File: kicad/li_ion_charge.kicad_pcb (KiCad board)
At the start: 2 copper layers, 31.9 x 25.9 mm, 18 parts, among them P101 USB_B, P102 CONN_01X02, P103 CONN_01X02, U101 MCP73834-FCI/UN

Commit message: add a couple vias
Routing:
- net (no net): track 0.97 -> 5.54 mm, vias 0 -> 3
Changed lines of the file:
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@@
     (links 38)
     (no_connects 0)
-    (area 86.062199 43.772899 177.985734 113.985733)
+    (area 86.062199 43.772899 177.310734 113.985733)
     (thickness 1.6)
     (drawings 6)
-    (tracks 54)
+    (tracks 59)
     (zones 0)
     (modules 18)
@@
   )
   (setup
-    (last_trace_width 0.3048)
+    (last_trace_width 0.6096)
     (user_trace_width 0.3048)
     (user_trace_width 0.6096)
@@
   (segment (start 86.3396 44.0503) (end 86.3396 44.7396) (width 0.25) (layer F.Cu) (net 0))
   (segment (start 96.6 58.05) (end 96.4 58.25) (width 0.25) (layer F.Cu) (net 0))
+  (via (at 144.018 87.63) (size 0.6858) (drill 0.3302) (layers F.Cu B.Cu) (net 0))
+  (via (at 144.018 92.202) (size 0.6858) (drill 0.3302) (layers F.Cu B.Cu) (net 0))
+  (segment (start 144.018 92.202) (end 144.018 90.17) (width 0.6096) (layer F.Cu) (net 0))
+  (via (at 144.018 90.17) (size 0.6858) (drill 0.3302) (layers F.Cu B.Cu) (net 0))
+  (segment (start 144.018 90.17) (end 144.018 87.63) (width 0.6096) (layer B.Cu) (net 0))
   (segment (start 167.125 102.875) (end 169.05 102.875) (width 0.3048) (layer F.Cu) (net 1))
   (segment (start 168.325 103.75) (end 157.825 103.75) (width 0.3048) (layer B.Cu) (net 1))
@@
   (segment (start 159.7 94.65) (end 161 94.65) (width 0.25) (layer F.Cu) (net 6))
   (segment (start 158.875 93.825) (end 159.7 94.65) (width 0.25) (layer F.Cu) (net 6))
-  (segment (start 144 93.975) (end 144 96) (width 0.3048) (layer F.Cu) (net 8))
-  (segment (start 143.875 93.85) (end 144 93.975) (width 0.3048) (layer F.Cu) (net 8))
-  (via (at 143.875 93.85) (size 0.6858) (drill 0.3302) (layers F.Cu B.Cu) (net 8))
-  (segment (start 143.875 93.8) (end 143.875 93.85) (width 0.3048) (layer B.Cu) (net 8))
-  (segment (start 144.6 93.075) (end 143.875 93.8) (width 0.6096) (layer B.Cu) (net 8))
+  (segment (start 144.143 94.105) (end 144 96) (width 0.3048) (layer F.Cu) (net 8))
+  (via (at 160.075 93.1) (size 0.6858) (drill 0.3302) (layers F.Cu B.Cu) (net 8))
+  (segment (start 160.075 93.1) (end 160.05 93.075) (width 0.3048) (layer B.Cu) (net 8))
   (segment (start 160.05 93.075) (end 144.6 93.075) (width 0.6096) (layer B.Cu) (net 8))
-  (segment (start 160.075 93.1) (end 160.05 93.075) (width 0.3048) (layer B.Cu) (net 8))
-  (via (at 160.075 93.1) (size 0.6858) (drill 0.3302) (layers F.Cu B.Cu) (net 8))
+  (segment (start 144.6 93.075) (end 144.018 93.93) (width 0.6096) (layer B.Cu) (net 8))
+  (segment (start 144.018 93.93) (end 144.018 93.98) (width 0.3048) (layer B.Cu) (net 8))
+  (via (at 144.018 93.98) (size 0.6858) (drill 0.3302) (layers F.Cu B.Cu) (net 8))
+  (segment (start 144.018 93.98) (end 144.143 94.105) (width 0.3048) (layer F.Cu) (net 8))
   (segment (start 143.9 107) (end 143.9 108.9) (width 0.3048) (layer F.Cu) (net 8))
   (segment (start 143.9 108.9) (end 146.175 111.175) (width 0.3048) (layer F.Cu) (net 8))

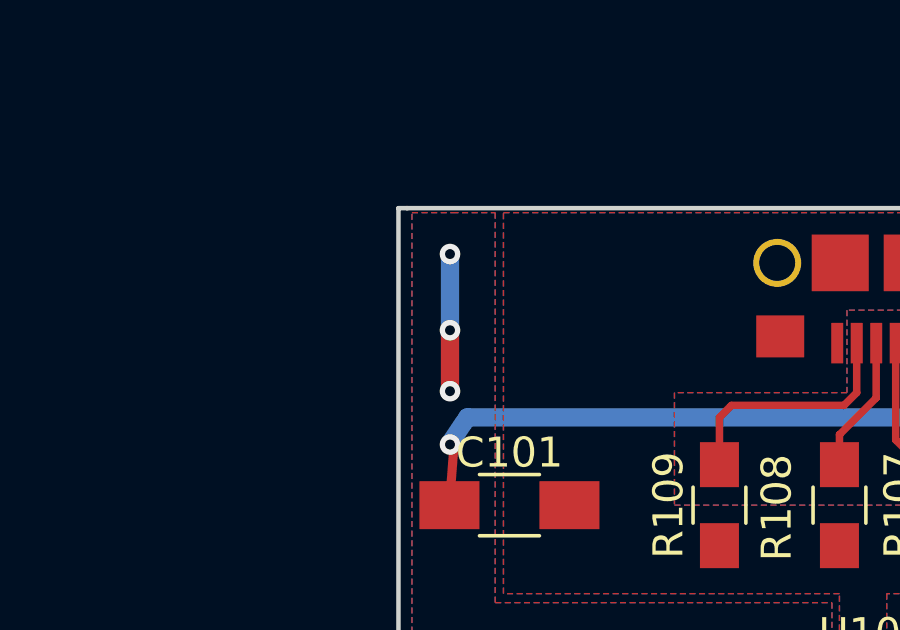
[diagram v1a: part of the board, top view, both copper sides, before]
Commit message: add stitching via footprint
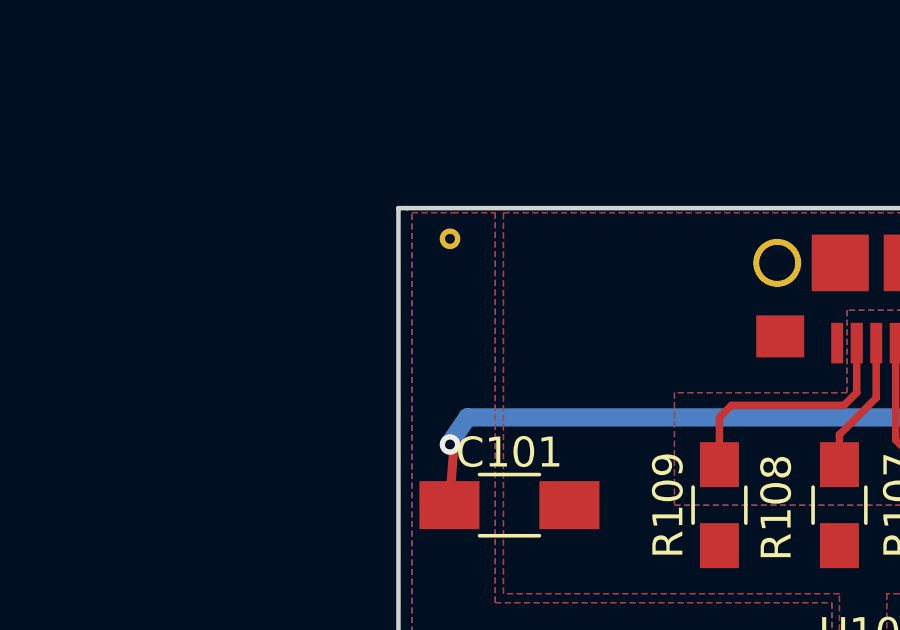
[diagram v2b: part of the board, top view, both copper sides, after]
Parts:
- added REF**: stitching_via, li_ion_charge_library:stitching_via, F.Cu at (144.0, 87.1)
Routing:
- net (no net): track 5.54 -> 0.97 mm, vias 3 -> 0
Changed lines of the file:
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@@
 (kicad_pcb (version 4) (host pcbnew 4.0.6-e0-6349~53~ubuntu14.04.1)
   (general
-    (links 38)
+    (links 39)
     (no_connects 0)
     (area 86.062199 43.772899 177.310734 113.985733)
     (thickness 1.6)
     (drawings 6)
-    (tracks 59)
+    (tracks 54)
     (zones 0)
-    (modules 18)
+    (modules 19)
     (nets 16)
   )
@@
     (mod_text_size 1 1)
     (mod_text_width 0.15)
-    (pad_size 1.524 1.524)
-    (pad_drill 0.762)
+    (pad_size 0.6858 0.6858)
+    (pad_drill 0.3302)
     (pad_to_mask_clearance 0)
     (aux_axis_origin 0 0)
@@
     )
   )
+  (module li_ion_charge_library:stitching_via (layer F.Cu)
+    (at 144.018 87.122)
+    (fp_text reference REF** (at 0.0762 0.9779) (layer F.SilkS) hide
+      (effects (font (size 1 1) (thickness 0.15)))
+    )
+    (fp_text value stitching_via (at 0 -2.54) (layer F.Fab) hide
+      (effects (font (size 1 1) (thickness 0.15)))
+    )
+    (pad 1 thru_hole circle (at 0 0) (size 0.6858 0.6858) (drill 0.3302) (layers *.Cu)
+      (net 8 /VIN))
+  )
   (gr_line (start 142.3 86.1) (end 142.6 86.1) (angle 90) (layer Edge.Cuts) (width 0.15))
   (gr_line (start 142.3 111.95) (end 142.3 86.1) (angle 90) (layer Edge.Cuts) (width 0.15))
@@
   (segment (start 86.3396 44.0503) (end 86.3396 44.7396) (width 0.25) (layer F.Cu) (net 0))
   (segment (start 96.6 58.05) (end 96.4 58.25) (width 0.25) (layer F.Cu) (net 0))
-  (via (at 144.018 87.63) (size 0.6858) (drill 0.3302) (layers F.Cu B.Cu) (net 0))
-  (via (at 144.018 92.202) (size 0.6858) (drill 0.3302) (layers F.Cu B.Cu) (net 0))
-  (segment (start 144.018 92.202) (end 144.018 90.17) (width 0.6096) (layer F.Cu) (net 0))
-  (via (at 144.018 90.17) (size 0.6858) (drill 0.3302) (layers F.Cu B.Cu) (net 0))
-  (segment (start 144.018 90.17) (end 144.018 87.63) (width 0.6096) (layer B.Cu) (net 0))
   (segment (start 167.125 102.875) (end 169.05 102.875) (width 0.3048) (layer F.Cu) (net 1))
   (segment (start 168.325 103.75) (end 157.825 103.75) (width 0.3048) (layer B.Cu) (net 1))

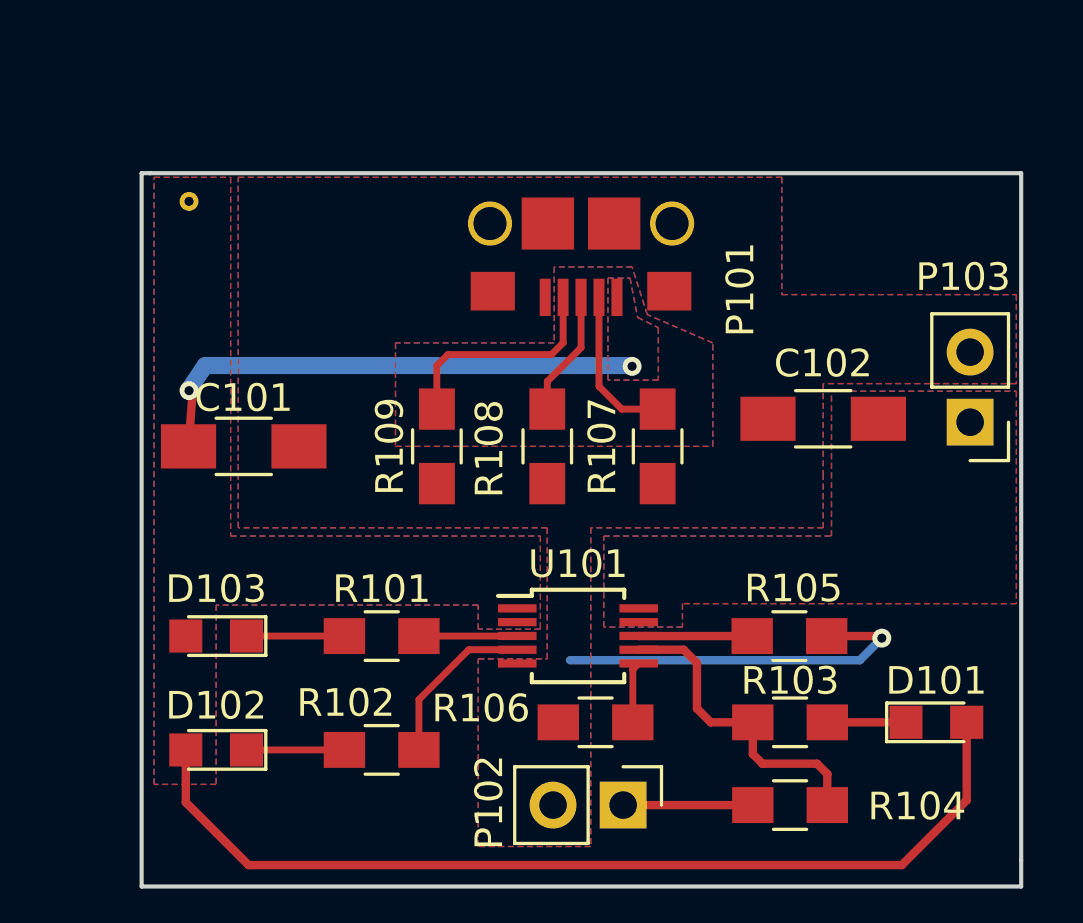
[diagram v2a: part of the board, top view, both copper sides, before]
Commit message: Add gerbers, and order boards from Osh Park
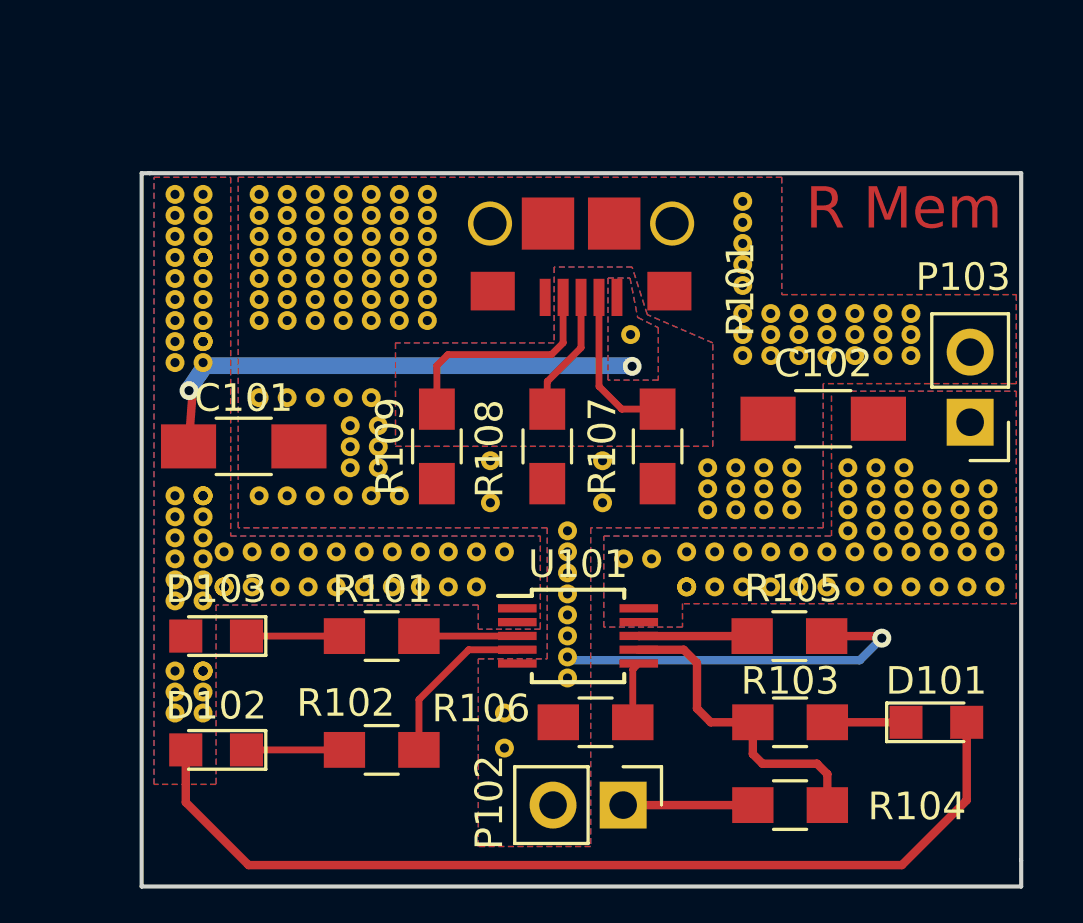
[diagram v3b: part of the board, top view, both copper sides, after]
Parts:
- added REF**: stitching_via, li_ion_charge_library:stitching_via, F.Cu at (173.0, 99.1)
- added REF**: stitching_via, li_ion_charge_library:stitching_via, F.Cu at (169.9, 99.1)
- added REF**: stitching_via, li_ion_charge_library:stitching_via, F.Cu at (154.9, 98.0)
- added REF**: stitching_via, li_ion_charge_library:stitching_via, F.Cu at (154.9, 96.5)
- added REF**: stitching_via, li_ion_charge_library:stitching_via, F.Cu at (151.6, 97.8)
- added REF**: stitching_via, li_ion_charge_library:stitching_via, F.Cu at (150.6, 97.8)
- added REF**: stitching_via, li_ion_charge_library:stitching_via, F.Cu at (149.6, 97.8)
- added REF**: stitching_via, li_ion_charge_library:stitching_via, F.Cu at (148.6, 97.8)
- added REF**: stitching_via, li_ion_charge_library:stitching_via, F.Cu at (147.6, 97.8)
- added REF**: stitching_via, li_ion_charge_library:stitching_via, F.Cu at (150.9, 96.8)
- added REF**: stitching_via, li_ion_charge_library:stitching_via, F.Cu at (149.9, 96.8)
- added REF**: stitching_via, li_ion_charge_library:stitching_via, F.Cu at (150.9, 96.0)
- added REF**: stitching_via, li_ion_charge_library:stitching_via, F.Cu at (168.9, 99.1)
- added REF**: stitching_via, li_ion_charge_library:stitching_via, F.Cu at (149.9, 96.0)
- added REF**: stitching_via, li_ion_charge_library:stitching_via, F.Cu at (150.9, 95.2)
- added REF**: stitching_via, li_ion_charge_library:stitching_via, F.Cu at (149.9, 95.2)
- added REF**: stitching_via, li_ion_charge_library:stitching_via, F.Cu at (146.6, 97.8)
- added REF**: stitching_via, li_ion_charge_library:stitching_via, F.Cu at (150.6, 94.2)
- added REF**: stitching_via, li_ion_charge_library:stitching_via, F.Cu at (149.6, 94.2)
- added REF**: stitching_via, li_ion_charge_library:stitching_via, F.Cu at (148.6, 94.2)
- added REF**: stitching_via, li_ion_charge_library:stitching_via, F.Cu at (147.6, 94.2)
- added REF**: stitching_via, li_ion_charge_library:stitching_via, F.Cu at (146.6, 94.2)
- added REF**: stitching_via, li_ion_charge_library:stitching_via, F.Cu at (152.7, 91.4)
- added REF**: stitching_via, li_ion_charge_library:stitching_via, F.Cu at (167.9, 99.1)
- added REF**: stitching_via, li_ion_charge_library:stitching_via, F.Cu at (151.6, 91.4)
- added REF**: stitching_via, li_ion_charge_library:stitching_via, F.Cu at (150.6, 91.4)
- added REF**: stitching_via, li_ion_charge_library:stitching_via, F.Cu at (149.6, 91.4)
- added REF**: stitching_via, li_ion_charge_library:stitching_via, F.Cu at (148.6, 91.4)
- added REF**: stitching_via, li_ion_charge_library:stitching_via, F.Cu at (147.6, 91.4)
- added REF**: stitching_via, li_ion_charge_library:stitching_via, F.Cu at (146.6, 91.4)
- added REF**: stitching_via, li_ion_charge_library:stitching_via, F.Cu at (152.7, 90.7)
- added REF**: stitching_via, li_ion_charge_library:stitching_via, F.Cu at (151.6, 90.7)
- added REF**: stitching_via, li_ion_charge_library:stitching_via, F.Cu at (150.6, 90.7)
- added REF**: stitching_via, li_ion_charge_library:stitching_via, F.Cu at (149.6, 90.7)
- added REF**: stitching_via, li_ion_charge_library:stitching_via, F.Cu at (169.9, 98.3)
- added REF**: stitching_via, li_ion_charge_library:stitching_via, F.Cu at (148.6, 90.7)
- added REF**: stitching_via, li_ion_charge_library:stitching_via, F.Cu at (147.6, 90.7)
- added REF**: stitching_via, li_ion_charge_library:stitching_via, F.Cu at (146.6, 90.7)
- added REF**: stitching_via, li_ion_charge_library:stitching_via, F.Cu at (152.7, 89.9)
- added REF**: stitching_via, li_ion_charge_library:stitching_via, F.Cu at (151.6, 89.9)
- added REF**: stitching_via, li_ion_charge_library:stitching_via, F.Cu at (150.6, 89.9)
- added REF**: stitching_via, li_ion_charge_library:stitching_via, F.Cu at (149.6, 89.9)
- added REF**: stitching_via, li_ion_charge_library:stitching_via, F.Cu at (148.6, 89.9)
- added REF**: stitching_via, li_ion_charge_library:stitching_via, F.Cu at (147.6, 89.9)
- added REF**: stitching_via, li_ion_charge_library:stitching_via, F.Cu at (146.6, 89.9)
- added REF**: stitching_via, li_ion_charge_library:stitching_via, F.Cu at (168.9, 98.3)
- added REF**: stitching_via, li_ion_charge_library:stitching_via, F.Cu at (152.7, 89.2)
- added REF**: stitching_via, li_ion_charge_library:stitching_via, F.Cu at (151.6, 89.2)
- added REF**: stitching_via, li_ion_charge_library:stitching_via, F.Cu at (150.6, 89.2)
- added REF**: stitching_via, li_ion_charge_library:stitching_via, F.Cu at (149.6, 89.2)
- added REF**: stitching_via, li_ion_charge_library:stitching_via, F.Cu at (148.6, 89.2)
- added REF**: stitching_via, li_ion_charge_library:stitching_via, F.Cu at (147.6, 89.2)
- added REF**: stitching_via, li_ion_charge_library:stitching_via, F.Cu at (146.6, 89.2)
- added REF**: stitching_via, li_ion_charge_library:stitching_via, F.Cu at (152.7, 88.4)
- added REF**: stitching_via, li_ion_charge_library:stitching_via, F.Cu at (151.6, 88.4)
- added REF**: stitching_via, li_ion_charge_library:stitching_via, F.Cu at (150.6, 88.4)
- added REF**: stitching_via, li_ion_charge_library:stitching_via, F.Cu at (167.9, 98.3)
- added REF**: stitching_via, li_ion_charge_library:stitching_via, F.Cu at (149.6, 88.4)
- added REF**: stitching_via, li_ion_charge_library:stitching_via, F.Cu at (148.6, 88.4)
- added REF**: stitching_via, li_ion_charge_library:stitching_via, F.Cu at (147.6, 88.4)
- added REF**: stitching_via, li_ion_charge_library:stitching_via, F.Cu at (146.6, 88.4)
- added REF**: stitching_via, li_ion_charge_library:stitching_via, F.Cu at (152.7, 87.6)
- added REF**: stitching_via, li_ion_charge_library:stitching_via, F.Cu at (151.6, 87.6)
- added REF**: stitching_via, li_ion_charge_library:stitching_via, F.Cu at (150.6, 87.6)
- added REF**: stitching_via, li_ion_charge_library:stitching_via, F.Cu at (149.6, 87.6)
- added REF**: stitching_via, li_ion_charge_library:stitching_via, F.Cu at (148.6, 87.6)
- added REF**: stitching_via, li_ion_charge_library:stitching_via, F.Cu at (147.6, 87.6)
- added REF**: stitching_via, li_ion_charge_library:stitching_via, F.Cu at (169.9, 97.5)
- added REF**: stitching_via, li_ion_charge_library:stitching_via, F.Cu at (146.6, 87.6)
- added REF**: stitching_via, li_ion_charge_library:stitching_via, F.Cu at (152.7, 86.9)
- added REF**: stitching_via, li_ion_charge_library:stitching_via, F.Cu at (151.6, 86.9)
- added REF**: stitching_via, li_ion_charge_library:stitching_via, F.Cu at (150.6, 86.9)
- added REF**: stitching_via, li_ion_charge_library:stitching_via, F.Cu at (149.6, 86.9)
- added REF**: stitching_via, li_ion_charge_library:stitching_via, F.Cu at (148.6, 86.9)
- added REF**: stitching_via, li_ion_charge_library:stitching_via, F.Cu at (147.6, 86.9)
- added REF**: stitching_via, li_ion_charge_library:stitching_via, F.Cu at (146.6, 86.9)
- added REF**: stitching_via, li_ion_charge_library:stitching_via, F.Cu at (155.4, 99.8)
- added REF**: stitching_via, li_ion_charge_library:stitching_via, F.Cu at (154.4, 101.1)
- added REF**: stitching_via, li_ion_charge_library:stitching_via, F.Cu at (168.9, 97.5)
- added REF**: stitching_via, li_ion_charge_library:stitching_via, F.Cu at (153.4, 101.1)
- added REF**: stitching_via, li_ion_charge_library:stitching_via, F.Cu at (152.4, 101.1)
- added REF**: stitching_via, li_ion_charge_library:stitching_via, F.Cu at (151.4, 101.1)
- added REF**: stitching_via, li_ion_charge_library:stitching_via, F.Cu at (150.4, 101.1)
- added REF**: stitching_via, li_ion_charge_library:stitching_via, F.Cu at (149.4, 101.1)
- added REF**: stitching_via, li_ion_charge_library:stitching_via, F.Cu at (148.3, 101.1)
- added REF**: stitching_via, li_ion_charge_library:stitching_via, F.Cu at (147.3, 101.1)
- added REF**: stitching_via, li_ion_charge_library:stitching_via, F.Cu at (146.3, 101.1)
- added REF** (x2): stitching_via, li_ion_charge_library:stitching_via, F.Cu at (145.3, 101.1)
- added REF**: stitching_via, li_ion_charge_library:stitching_via, F.Cu at (154.4, 99.8)
- added REF**: stitching_via, li_ion_charge_library:stitching_via, F.Cu at (167.9, 97.5)
- added REF**: stitching_via, li_ion_charge_library:stitching_via, F.Cu at (153.4, 99.8)
- added REF**: stitching_via, li_ion_charge_library:stitching_via, F.Cu at (152.4, 99.8)
- added REF**: stitching_via, li_ion_charge_library:stitching_via, F.Cu at (151.4, 99.8)
- added REF**: stitching_via, li_ion_charge_library:stitching_via, F.Cu at (150.4, 99.8)
- added REF**: stitching_via, li_ion_charge_library:stitching_via, F.Cu at (149.4, 99.8)
- added REF**: stitching_via, li_ion_charge_library:stitching_via, F.Cu at (148.3, 99.8)
- added REF**: stitching_via, li_ion_charge_library:stitching_via, F.Cu at (147.3, 99.8)
- added REF**: stitching_via, li_ion_charge_library:stitching_via, F.Cu at (146.3, 99.8)
- added REF**: stitching_via, li_ion_charge_library:stitching_via, F.Cu at (145.3, 99.8)
- added REF**: stitching_via, li_ion_charge_library:stitching_via, F.Cu at (169.9, 96.8)
- added REF**: stitching_via, li_ion_charge_library:stitching_via, F.Cu at (144.5, 105.7)
- added REF**: stitching_via, li_ion_charge_library:stitching_via, F.Cu at (143.5, 105.7)
- added REF**: stitching_via, li_ion_charge_library:stitching_via, F.Cu at (144.5, 104.9)
- added REF**: stitching_via, li_ion_charge_library:stitching_via, F.Cu at (143.5, 104.9)
- added REF** (x2): stitching_via, li_ion_charge_library:stitching_via, F.Cu at (144.5, 104.1)
- added REF**: stitching_via, li_ion_charge_library:stitching_via, F.Cu at (143.5, 104.1)
- added REF**: stitching_via, li_ion_charge_library:stitching_via, F.Cu at (144.5, 101.6)
- added REF**: stitching_via, li_ion_charge_library:stitching_via, F.Cu at (143.5, 101.6)
- added REF**: stitching_via, li_ion_charge_library:stitching_via, F.Cu at (144.5, 100.8)
- added REF**: stitching_via, li_ion_charge_library:stitching_via, F.Cu at (172.0, 99.1)
- added REF**: stitching_via, li_ion_charge_library:stitching_via, F.Cu at (168.9, 96.8)
- added REF**: stitching_via, li_ion_charge_library:stitching_via, F.Cu at (143.5, 100.8)
- added REF**: stitching_via, li_ion_charge_library:stitching_via, F.Cu at (144.5, 100.1)
- added REF**: stitching_via, li_ion_charge_library:stitching_via, F.Cu at (143.5, 100.1)
- added REF**: stitching_via, li_ion_charge_library:stitching_via, F.Cu at (144.5, 99.3)
- added REF**: stitching_via, li_ion_charge_library:stitching_via, F.Cu at (143.5, 99.3)
- added REF**: stitching_via, li_ion_charge_library:stitching_via, F.Cu at (144.5, 98.6)
- added REF**: stitching_via, li_ion_charge_library:stitching_via, F.Cu at (143.5, 98.6)
- added REF** (x2): stitching_via, li_ion_charge_library:stitching_via, F.Cu at (144.5, 97.8)
- added REF**: stitching_via, li_ion_charge_library:stitching_via, F.Cu at (143.5, 97.8)
- added REF**: stitching_via, li_ion_charge_library:stitching_via, F.Cu at (167.9, 96.8)
- added REF**: stitching_via, li_ion_charge_library:stitching_via, F.Cu at (144.5, 93.0)
- added REF**: stitching_via, li_ion_charge_library:stitching_via, F.Cu at (143.5, 93.0)
- added REF** (x2): stitching_via, li_ion_charge_library:stitching_via, F.Cu at (144.5, 92.2)
- added REF**: stitching_via, li_ion_charge_library:stitching_via, F.Cu at (143.5, 92.2)
- added REF**: stitching_via, li_ion_charge_library:stitching_via, F.Cu at (144.5, 91.4)
- added REF**: stitching_via, li_ion_charge_library:stitching_via, F.Cu at (143.5, 91.4)
- added REF**: stitching_via, li_ion_charge_library:stitching_via, F.Cu at (144.5, 90.7)
- added REF**: stitching_via, li_ion_charge_library:stitching_via, F.Cu at (143.5, 90.7)
- added REF**: stitching_via, li_ion_charge_library:stitching_via, F.Cu at (144.5, 89.9)
- added REF**: stitching_via, li_ion_charge_library:stitching_via, F.Cu at (173.2, 101.1)
- added REF**: stitching_via, li_ion_charge_library:stitching_via, F.Cu at (143.5, 89.9)
- added REF** (x2): stitching_via, li_ion_charge_library:stitching_via, F.Cu at (144.5, 89.2)
- added REF**: stitching_via, li_ion_charge_library:stitching_via, F.Cu at (143.5, 89.2)
- added REF**: stitching_via, li_ion_charge_library:stitching_via, F.Cu at (144.5, 88.4)
- added REF**: stitching_via, li_ion_charge_library:stitching_via, F.Cu at (143.5, 88.4)
- added REF**: stitching_via, li_ion_charge_library:stitching_via, F.Cu at (143.5, 87.6)
- added REF**: stitching_via, li_ion_charge_library:stitching_via, F.Cu at (144.5, 87.6)
- added REF**: stitching_via, li_ion_charge_library:stitching_via, F.Cu at (143.5, 86.9)
- added REF**: stitching_via, li_ion_charge_library:stitching_via, F.Cu at (172.2, 101.1)
- added REF**: stitching_via, li_ion_charge_library:stitching_via, F.Cu at (171.2, 101.1)
- added REF**: stitching_via, li_ion_charge_library:stitching_via, F.Cu at (170.2, 101.1)
- added REF**: stitching_via, li_ion_charge_library:stitching_via, F.Cu at (169.2, 101.1)
- added REF**: stitching_via, li_ion_charge_library:stitching_via, F.Cu at (168.1, 101.1)
- added REF**: stitching_via, li_ion_charge_library:stitching_via, F.Cu at (167.1, 101.1)
- added REF**: stitching_via, li_ion_charge_library:stitching_via, F.Cu at (166.1, 101.1)
- added REF**: stitching_via, li_ion_charge_library:stitching_via, F.Cu at (170.9, 99.1)
- added REF**: stitching_via, li_ion_charge_library:stitching_via, F.Cu at (165.1, 101.1)
- added REF**: stitching_via, li_ion_charge_library:stitching_via, F.Cu at (164.1, 101.1)
- added REF**: stitching_via, li_ion_charge_library:stitching_via, F.Cu at (163.1, 101.1)
- added REF** (x2): stitching_via, li_ion_charge_library:stitching_via, F.Cu at (162.1, 101.1)
- added REF**: stitching_via, li_ion_charge_library:stitching_via, F.Cu at (173.2, 99.8)
- added REF**: stitching_via, li_ion_charge_library:stitching_via, F.Cu at (172.2, 99.8)
- added REF**: stitching_via, li_ion_charge_library:stitching_via, F.Cu at (171.2, 99.8)
- added REF**: stitching_via, li_ion_charge_library:stitching_via, F.Cu at (170.2, 99.8)
- added REF**: stitching_via, li_ion_charge_library:stitching_via, F.Cu at (169.2, 99.8)
- added REF**: stitching_via, li_ion_charge_library:stitching_via, F.Cu at (168.1, 99.8)
- added REF**: stitching_via, li_ion_charge_library:stitching_via, F.Cu at (173.0, 98.3)
- added REF**: stitching_via, li_ion_charge_library:stitching_via, F.Cu at (167.1, 99.8)
- added REF**: stitching_via, li_ion_charge_library:stitching_via, F.Cu at (166.1, 99.8)
- added REF**: stitching_via, li_ion_charge_library:stitching_via, F.Cu at (165.1, 99.8)
- added REF**: stitching_via, li_ion_charge_library:stitching_via, F.Cu at (164.1, 99.8)
- added REF**: stitching_via, li_ion_charge_library:stitching_via, F.Cu at (163.1, 99.8)
- added REF**: stitching_via, li_ion_charge_library:stitching_via, F.Cu at (162.1, 99.8)
- added REF**: stitching_via, li_ion_charge_library:stitching_via, F.Cu at (160.8, 100.1)
- added REF**: stitching_via, li_ion_charge_library:stitching_via, F.Cu at (159.8, 100.1)
- added REF**: stitching_via, li_ion_charge_library:stitching_via, F.Cu at (170.2, 92.7)
- added REF**: stitching_via, li_ion_charge_library:stitching_via, F.Cu at (172.0, 98.3)
- added REF**: stitching_via, li_ion_charge_library:stitching_via, F.Cu at (169.2, 92.7)
- added REF**: stitching_via, li_ion_charge_library:stitching_via, F.Cu at (168.1, 92.7)
- added REF**: stitching_via, li_ion_charge_library:stitching_via, F.Cu at (167.1, 92.7)
- added REF**: stitching_via, li_ion_charge_library:stitching_via, F.Cu at (166.1, 92.7)
- added REF**: stitching_via, li_ion_charge_library:stitching_via, F.Cu at (165.1, 92.7)
- added REF**: stitching_via, li_ion_charge_library:stitching_via, F.Cu at (164.1, 92.7)
- added REF**: stitching_via, li_ion_charge_library:stitching_via, F.Cu at (170.2, 91.9)
- added REF**: stitching_via, li_ion_charge_library:stitching_via, F.Cu at (169.2, 91.9)
- added REF**: stitching_via, li_ion_charge_library:stitching_via, F.Cu at (168.1, 91.9)
- added REF**: stitching_via, li_ion_charge_library:stitching_via, F.Cu at (167.1, 91.9)
- added REF**: stitching_via, li_ion_charge_library:stitching_via, F.Cu at (170.9, 98.3)
- added REF**: stitching_via, li_ion_charge_library:stitching_via, F.Cu at (166.1, 91.9)
- added REF**: stitching_via, li_ion_charge_library:stitching_via, F.Cu at (165.1, 91.9)
- added REF**: stitching_via, li_ion_charge_library:stitching_via, F.Cu at (164.1, 91.9)
- added REF**: stitching_via, li_ion_charge_library:stitching_via, F.Cu at (170.2, 91.2)
- added REF**: stitching_via, li_ion_charge_library:stitching_via, F.Cu at (169.2, 91.2)
- added REF**: stitching_via, li_ion_charge_library:stitching_via, F.Cu at (168.1, 91.2)
- added REF**: stitching_via, li_ion_charge_library:stitching_via, F.Cu at (167.1, 91.2)
- added REF**: stitching_via, li_ion_charge_library:stitching_via, F.Cu at (166.1, 91.2)
- added REF**: stitching_via, li_ion_charge_library:stitching_via, F.Cu at (165.1, 91.2)
- added REF**: stitching_via, li_ion_charge_library:stitching_via, F.Cu at (164.1, 91.2)
- added REF**: stitching_via, li_ion_charge_library:stitching_via, F.Cu at (173.0, 97.5)
- added REF**: stitching_via, li_ion_charge_library:stitching_via, F.Cu at (164.1, 90.2)
- added REF**: stitching_via, li_ion_charge_library:stitching_via, F.Cu at (164.1, 89.4)
- added REF**: stitching_via, li_ion_charge_library:stitching_via, F.Cu at (164.1, 88.6)
- added REF**: stitching_via, li_ion_charge_library:stitching_via, F.Cu at (164.1, 87.9)
- added REF**: stitching_via, li_ion_charge_library:stitching_via, F.Cu at (164.1, 87.1)
- added REF**: stitching_via, li_ion_charge_library:stitching_via, F.Cu at (160.0, 91.9)
- added REF**: stitching_via, li_ion_charge_library:stitching_via, F.Cu at (165.9, 98.3)
- added REF**: stitching_via, li_ion_charge_library:stitching_via, F.Cu at (164.8, 98.3)
- added REF**: stitching_via, li_ion_charge_library:stitching_via, F.Cu at (163.8, 98.3)
- added REF**: stitching_via, li_ion_charge_library:stitching_via, F.Cu at (162.8, 98.3)
- added REF**: stitching_via, li_ion_charge_library:stitching_via, F.Cu at (172.0, 97.5)
- added REF**: stitching_via, li_ion_charge_library:stitching_via, F.Cu at (165.9, 97.5)
- added REF**: stitching_via, li_ion_charge_library:stitching_via, F.Cu at (164.8, 97.5)
- added REF**: stitching_via, li_ion_charge_library:stitching_via, F.Cu at (163.8, 97.5)
- added REF**: stitching_via, li_ion_charge_library:stitching_via, F.Cu at (162.8, 97.5)
- added REF**: stitching_via, li_ion_charge_library:stitching_via, F.Cu at (165.9, 96.8)
- added REF**: stitching_via, li_ion_charge_library:stitching_via, F.Cu at (164.8, 96.8)
- added REF**: stitching_via, li_ion_charge_library:stitching_via, F.Cu at (163.8, 96.8)
- added REF**: stitching_via, li_ion_charge_library:stitching_via, F.Cu at (162.8, 96.8)
- added REF**: stitching_via, li_ion_charge_library:stitching_via, F.Cu at (155.4, 106.9)
- added REF**: stitching_via, li_ion_charge_library:stitching_via, F.Cu at (155.4, 105.7)
- added REF**: stitching_via, li_ion_charge_library:stitching_via, F.Cu at (170.9, 97.5)
- added REF**: stitching_via, li_ion_charge_library:stitching_via, F.Cu at (157.7, 104.4)
- added REF**: stitching_via, li_ion_charge_library:stitching_via, F.Cu at (157.7, 103.6)
- added REF**: stitching_via, li_ion_charge_library:stitching_via, F.Cu at (157.7, 102.9)
- added REF**: stitching_via, li_ion_charge_library:stitching_via, F.Cu at (157.7, 102.1)
- added REF**: stitching_via, li_ion_charge_library:stitching_via, F.Cu at (157.7, 101.3)
- added REF**: stitching_via, li_ion_charge_library:stitching_via, F.Cu at (157.7, 100.6)
- added REF**: stitching_via, li_ion_charge_library:stitching_via, F.Cu at (157.7, 99.8)
- added REF**: stitching_via, li_ion_charge_library:stitching_via, F.Cu at (157.7, 99.1)
- added REF**: stitching_via, li_ion_charge_library:stitching_via, F.Cu at (159.0, 98.0)
- added REF**: stitching_via, li_ion_charge_library:stitching_via, F.Cu at (159.0, 96.5)
- moved REF** 0.57 mm to (144.5, 86.9)
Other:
- board text added: "Lithium Ion Charger"
- board text added: "R Mem"
